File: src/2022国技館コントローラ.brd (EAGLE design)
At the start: 48 parts

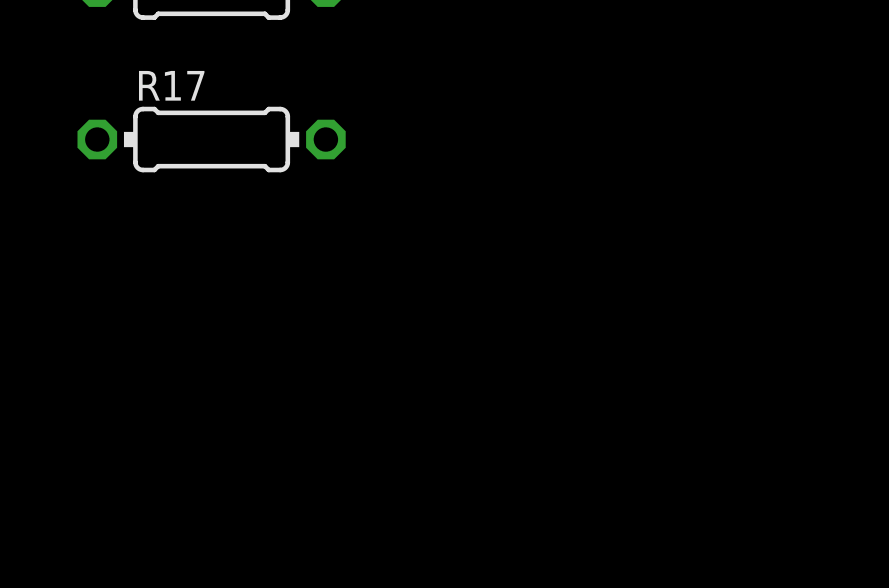
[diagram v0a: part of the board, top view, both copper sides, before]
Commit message: 国技館コントローラの追加
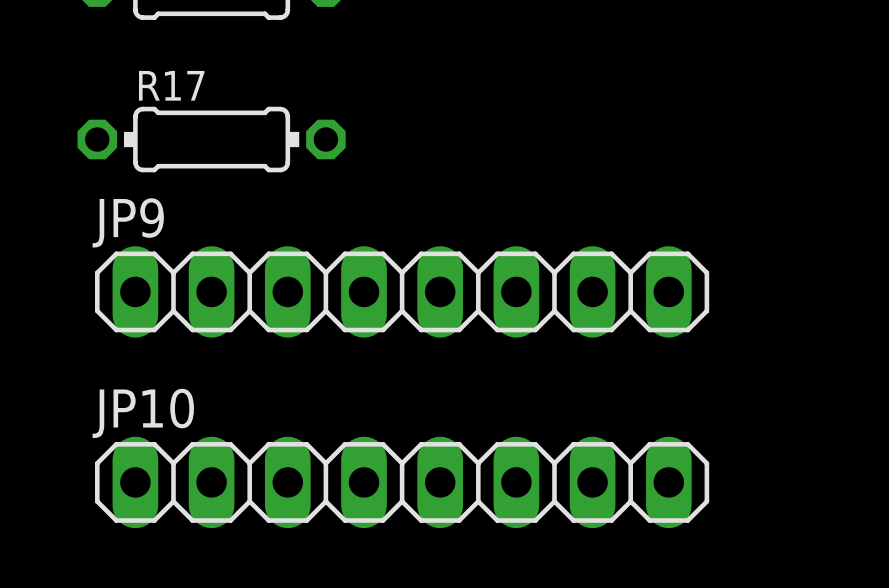
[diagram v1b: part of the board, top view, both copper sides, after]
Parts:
- added JP10, JP9: (no value), pinhead:1X08
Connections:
- new net BUSY: JP9.1
- new net RESET: JP9.8
- new net RX: JP9.4
- new net SLEEP: JP10.2
- new net STATUS: JP9.6
- new net TX: JP10.3
- new net VCC: JP9.7
- new net XMIT: JP9.2
- net GND: now also JP10.8
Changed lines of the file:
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@@
 <attribute name="VALUE" x="-181.9656" y="-156.6926" size="0.9906" layer="27" ratio="10"/>
+</element>
+<element name="JP9" library="pinhead" library_urn="urn:adsk.eagle:library:325" package="1X08" package3d_urn="urn:adsk.eagle:package:22409/2" value="" x="-173.99" y="-161.29" smashed="yes">
+<attribute name="NAME" x="-184.2262" y="-159.4612" size="1.27" layer="25" ratio="10"/>
+<attribute name="POPULARITY" value="67" x="-173.99" y="-161.29" size="1.778" layer="27" display="off"/>
+<attribute name="VALUE" x="-184.15" y="-164.465" size="1.27" layer="27"/>
+</element>
+<element name="JP10" library="pinhead" library_urn="urn:adsk.eagle:library:325" package="1X08" package3d_urn="urn:adsk.eagle:package:22409/2" value="" x="-173.99" y="-167.64" smashed="yes">
+<attribute name="NAME" x="-184.2262" y="-165.8112" size="1.27" layer="25" ratio="10"/>
+<attribute name="POPULARITY" value="67" x="-173.99" y="-167.64" size="1.778" layer="27" display="off"/>
+<attribute name="VALUE" x="-184.15" y="-170.815" size="1.27" layer="27"/>
 </element>
 </elements>
@@
 <contactref element="LED4" pad="K"/>
 <contactref element="LED5" pad="K"/>
+<contactref element="JP10" pad="8"/>
 <wire x1="-176.53" y1="-68.58" x2="-176.53" y2="-73.66" width="0" layer="19" extent="1-1"/>
 <wire x1="-176.53" y1="-63.5" x2="-176.53" y2="-68.58" width="0" layer="19" extent="1-1"/>
@@
 <wire x1="-180.34" y1="-121.92" x2="-180.34" y2="-114.3" width="0" layer="19" extent="1-1"/>
 <wire x1="-180.34" y1="-129.54" x2="-180.34" y2="-121.92" width="0" layer="19" extent="1-1"/>
+<wire x1="-165.1" y1="-167.64" x2="-180.34" y2="-129.54" width="0" layer="19" extent="1-1"/>
 <wire x1="-58.42" y1="-19.05" x2="-176.53" y2="-38.1" width="0" layer="19" extent="1-1"/>
 <wire x1="-58.42" y1="-11.43" x2="-58.42" y2="-19.05" width="0" layer="19" extent="1-1"/>
@@
 <contactref element="R17" pad="1"/>
 </signal>
+<signal name="BUSY">
+<contactref element="JP9" pad="1"/>
+</signal>
+<signal name="XMIT">
+<contactref element="JP9" pad="2"/>
+</signal>
+<signal name="TX">
+<contactref element="JP10" pad="3"/>
+</signal>
+<signal name="RX">
+<contactref element="JP9" pad="4"/>
+</signal>
+<signal name="STATUS">
+<contactref element="JP9" pad="6"/>
+</signal>
+<signal name="VCC">
+<contactref element="JP9" pad="7"/>
+</signal>
+<signal name="RESET">
+<contactref element="JP9" pad="8"/>
+</signal>
+<signal name="SLEEP">
+<contactref element="JP10" pad="2"/>
+</signal>
 </signals>

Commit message: 「ｋ」コントローラ
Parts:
- added JP11, JP12: (no value), con-jst-xh (1):B5B-XH
- added SV1, SV2: (no value), con-ml:ML10
- added U$15: 02-JST, con-jst-xh (1):B2B-XH
- moved U$14 331.8 mm to (134.6, 71.1), turned to 180 degrees
- moved R8 328.9 mm to (110.5, 80.0), turned to 270 degrees
- moved R7 327.7 mm to (113.0, 77.5), turned to 270 degrees
- moved R6 326.7 mm to (115.6, 74.9), turned to 270 degrees
- moved R5 325.9 mm to (118.1, 72.4), turned to 270 degrees
- moved U$13 324.5 mm to (134.6, 78.7), turned to 180 degrees
- moved U$10 279.0 mm to (111.8, 88.9), turned to 180 degrees
- moved U$9 276.7 mm to (119.4, 88.9), turned to 180 degrees
- moved U$8 274.4 mm to (127.0, 88.9), turned to 180 degrees
- moved U$7 272.1 mm to (134.6, 88.9), turned to 180 degrees
- moved R1 237.2 mm to (25.4, 80.0), turned to 270 degrees
- moved R2 236.3 mm to (22.9, 77.5), turned to 270 degrees
- moved R3 235.5 mm to (20.3, 74.9), turned to 270 degrees
- moved R4 234.6 mm to (17.8, 72.4), turned to 270 degrees
- moved LED1 219.2 mm to (-12.7, 40.6)
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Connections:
- removed net VCC: JP9.7
- new net VIN: F411RE_LEFT.24, U$15.2
- net 3V3: now also F411RE_LEFT.16, JP9.7, SV1.2, SV2.2
- net BL1: now also F411RE_RIGHT.11
- net BL2: now also F411RE_RIGHT.13
- net BR1: now also F411RE_RIGHT.23
- net BR2: now also F411RE_RIGHT.25
- net BUSY: now also F411RE_RIGHT.24, SV1.10, SV2.10
- net CK1_DOWN: now also F411RE_RIGHT.21, U$4.1; no longer U$5.1
- net CK1_LEFT: now also F411RE_RIGHT.15
- net CK1_RIGHT: now also F411RE_RIGHT.17, U$5.1; no longer U$6.1
- net CK1_UP: now also F411RE_RIGHT.19, U$6.1; no longer U$4.1
- net CK2_DOWN: now also F411RE_RIGHT.33, U$10.1; no longer U$9.1
- net CK2_LEFT: now also F411RE_RIGHT.27, U$7.1; no longer U$8.1
- net CK2_RIGHT: now also F411RE_RIGHT.29, U$9.1; no longer U$10.1
- net CK2_UP: now also F411RE_RIGHT.31, U$8.1; no longer U$7.1
- net GND: now also F411RE_LEFT.8, SV1.3, SV2.3, U$15.1
- net L/R1: now also F411RE_LEFT.28
- net L/R2: now also F411RE_LEFT.32
- net LED1: now also F411RE_RIGHT.1, JP11.1, JP12.1
- net LED2: now also F411RE_RIGHT.3, JP11.2, JP12.2
- net LED3: now also F411RE_RIGHT.5, JP11.3, JP12.3
- net LED4: now also F411RE_RIGHT.2, JP11.4, JP12.4
- net LED5: now also F411RE_RIGHT.4, JP11.5, JP12.5
- net RESET: now also F411RE_RIGHT.30, SV1.9, SV2.9
- net RX: now also F411RE_LEFT.21, SV1.6, SV2.6
- net SLEEP: now also F411RE_RIGHT.22, SV1.7, SV2.7
- net STATUS: now also F411RE_RIGHT.28, SV1.4, SV2.4
- net TX: now also F411RE_LEFT.17, SV1.5, SV2.5
- net U/D1: now also F411RE_LEFT.30
- net U/D2: now also F411RE_LEFT.34
- net XMIT: now also F411RE_RIGHT.26, SV1.8, SV2.8
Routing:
- net 3V3: track 0.00 -> 64.6 mm

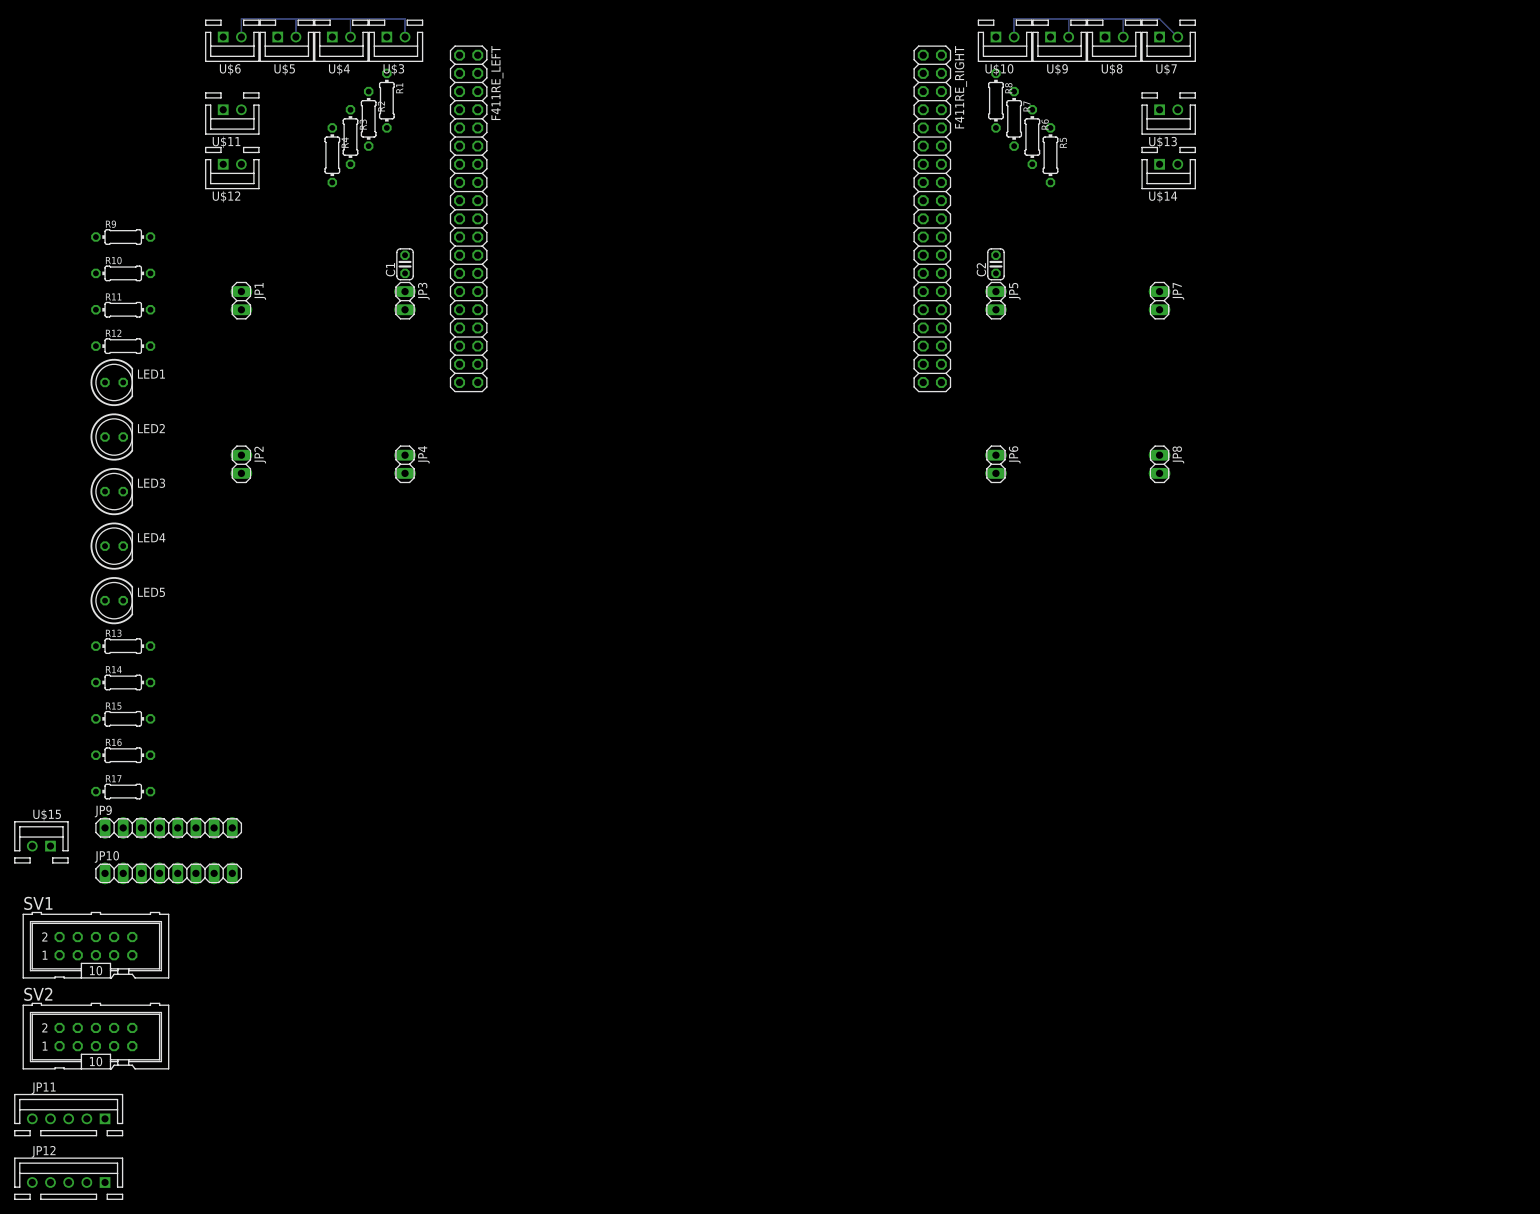
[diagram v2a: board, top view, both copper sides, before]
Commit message: 国技館コントローラ_配線の修正
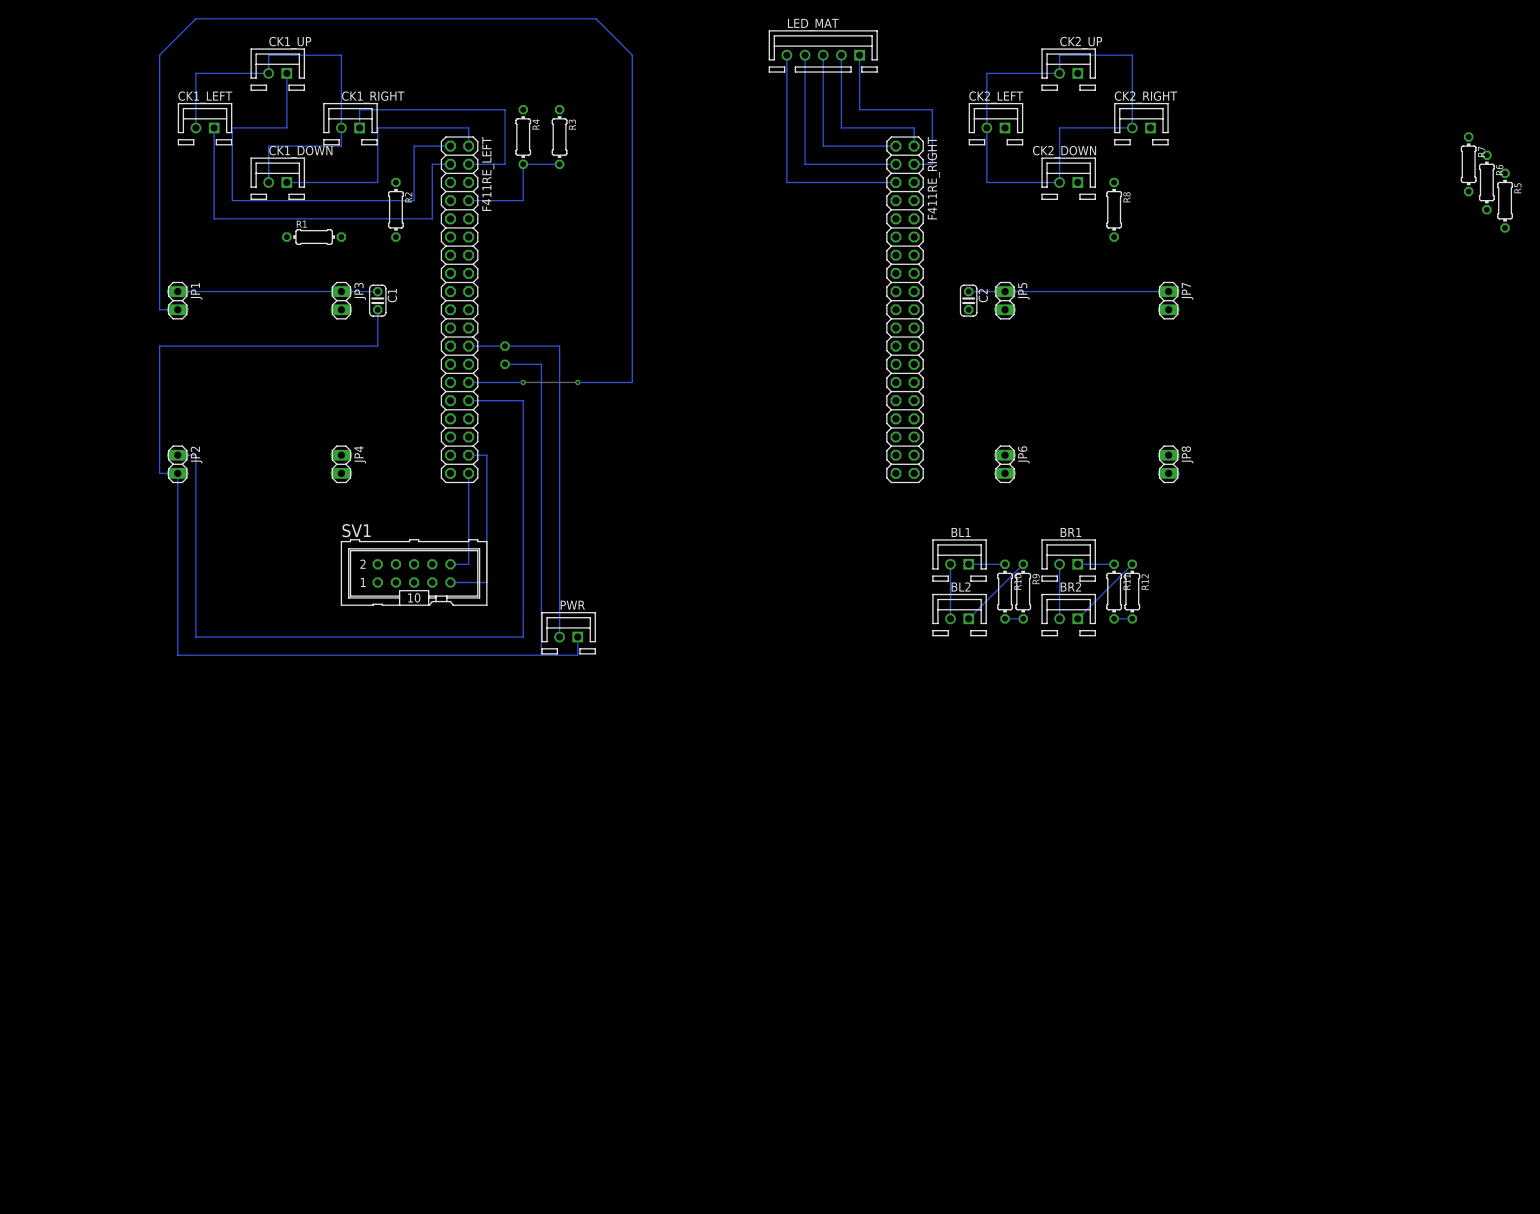
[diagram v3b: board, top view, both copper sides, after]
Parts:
- removed JP10, JP9: (no value), pinhead:1X08
- removed JP11, JP12: (no value), con-jst-xh (1):B5B-XH
- removed LED1, LED2, LED3, LED4, LED5: (no value), led:LED5MM
- removed R13, R14, R15, R16, R17: (no value), rcl:0204/7
- removed SV2: (no value), con-ml:ML10
- removed U$10, U$11, U$12, U$13, U$14, U$3, U$4, U$5, U$6, U$7, U$8, U$9: 02-JST, con-jst-xh:B2B-XH
- removed U$15: 02-JST, con-jst-xh (1):B2B-XH
- added BL1, BL2, BR1, BR2, CK1_DOWN, CK1_LEFT, CK1_RIGHT, CK1_UP, CK2_DOWN, CK2_LEFT, CK2_RIGHT, CK2_UP: 02-JST, con-jst-xh:B2B-XH
- added C3: 100nF, rcl:C025-024X044
- added LED_MAT: (no value), con-jst-xh (1):B5B-XH
- added PWR: 02-JST, con-jst-xh (1):B2B-XH
- R1, R10, R11, R12, R2, R3, R4, R5, R6, R7, R8, R9: value (none) -> 10k
- moved R12 145.1 mm to (129.5, 11.4), turned to 270 degrees
- moved R11 143.9 mm to (127.0, 11.4), turned to 270 degrees
- moved R9 135.1 mm to (114.3, 11.4), turned to 270 degrees
- moved R10 131.0 mm to (111.8, 11.4), turned to 270 degrees
- moved U$1 121.8 mm to (-8.89, 94.0), turned to 270 degrees
- moved U$2 118.6 mm to (68.6, 94.0), turned to 270 degrees
- moved SV1 68.5 mm to (29.2, 14.0)
- moved R5 63.8 mm to (181.6, 66.0)
- moved R6 63.8 mm to (179.1, 68.6)
- moved R7 63.8 mm to (176.5, 71.1)
- moved R3 29.2 mm to (49.5, 74.9)
- moved R4 26.8 mm to (44.5, 74.9)
- moved R8 22.5 mm to (127.0, 64.8)
- moved R1 21.6 mm to (15.2, 61.0), turned to 0 degrees
- moved R2 13.3 mm to (26.7, 64.8)
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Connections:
- removed net N$10: LED5.A, R17.2
- removed net N$6: LED1.A, R13.2
- removed net N$7: LED2.A, R14.2
- removed net N$8: LED3.A, R15.2
- removed net N$9: LED4.A, R16.2
- net 3V3: now also BL1.2, BL2.2, BR1.2, BR2.2, CK1_DOWN.2, CK1_LEFT.2, CK1_RIGHT.2, CK1_UP.2, CK2_DOWN.2, CK2_LEFT.2, CK2_RIGHT.2, CK2_UP.2; no longer JP9.7, SV2.2, U$10.2, U$11.2, U$12.2, U$13.2, U$14.2, U$3.2, U$4.2, U$5.2, U$6.2, U$7.2, U$8.2, U$9.2
- net BL1: now also BL1.1; no longer U$11.1
- net BL2: now also BL2.1; no longer U$12.1
- net BR1: now also BR1.1; no longer U$13.1
- net BR2: now also BR2.1; no longer U$14.1
- net BUSY: now also F411RE_LEFT.38; no longer F411RE_RIGHT.24, JP9.1, SV2.10
- net CK1_DOWN: now also CK1_DOWN.1, F411RE_LEFT.2; no longer F411RE_RIGHT.21, U$4.1
- net CK1_LEFT: now also CK1_LEFT.1, F411RE_LEFT.3; no longer F411RE_RIGHT.15, U$3.1
- net CK1_RIGHT: now also CK1_RIGHT.1, F411RE_LEFT.4; no longer F411RE_RIGHT.17, U$5.1
- net CK1_UP: now also CK1_UP.1, F411RE_LEFT.1; no longer F411RE_RIGHT.19, U$6.1
- net CK2_DOWN: now also CK2_DOWN.1; no longer U$10.1
- net CK2_LEFT: now also CK2_LEFT.1; no longer U$7.1
- net CK2_RIGHT: now also CK2_RIGHT.1; no longer U$9.1
- net CK2_UP: now also CK2_UP.1; no longer U$8.1
- net GND: now also C3.2, PWR.1; no longer JP10.8, LED1.K, LED2.K, LED3.K, LED4.K, LED5.K, SV2.3, U$15.1
- net LED1: now also F411RE_RIGHT.5, LED_MAT.5; no longer F411RE_RIGHT.1, JP11.1, JP12.1, R13.1
- net LED2: now also LED_MAT.4; no longer JP11.2, JP12.2, R14.1
- net LED3: now also F411RE_RIGHT.1, LED_MAT.3; no longer F411RE_RIGHT.5, JP11.3, JP12.3, R15.1
- net LED4: now also LED_MAT.2; no longer JP11.4, JP12.4, R16.1
- net LED5: now also LED_MAT.1; no longer JP11.5, JP12.5, R17.1
- net RESET: now also F411RE_LEFT.36; no longer F411RE_RIGHT.30, JP9.8, SV2.9
- net RX: no longer JP9.4, SV2.6
- net SLEEP: now also F411RE_LEFT.35; no longer F411RE_RIGHT.22, JP10.2, SV2.7
- net STATUS: now also F411RE_LEFT.37; no longer F411RE_RIGHT.28, JP9.6, SV2.4
- net TX: no longer JP10.3, SV2.5
- net VIN: now also C3.1, PWR.2; no longer U$15.2
- net XMIT: now also F411RE_LEFT.31; no longer F411RE_RIGHT.26, JP9.2, SV2.8
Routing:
- net GND: track 0.00 -> 208.3 mm
- net L/R1: track 0.00 -> 176.9 mm, vias 0 -> 2
- net 3V3: track 64.6 -> 205.7 mm
- net U/D1: track 0.00 -> 114.3 mm
- net CK1_UP: track 0.00 -> 63.5 mm
- net CK1_LEFT: track 0.00 -> 53.3 mm
- net VIN: track 0.00 -> 53.3 mm
- net CK1_DOWN: track 0.00 -> 35.6 mm
- net CK1_RIGHT: track 0.00 -> 35.6 mm
- net LED1: track 0.00 -> 33.0 mm
- net LED2: track 0.00 -> 27.9 mm
- net LED5: track 0.00 -> 27.9 mm
- net RESET: track 0.00 -> 25.4 mm
- net LED4: track 0.00 -> 22.9 mm
- net LED3: track 0.00 -> 22.9 mm
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
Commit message: [k]コントローラ
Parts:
- added U$3, U$4: 02-JST, con-jst-xh (1):B2B-XH
- moved R5 52.2 mm to (129.5, 62.2)
- moved R6 47.1 mm to (132.1, 64.8)
- moved R7 42.1 mm to (134.6, 67.3)
- moved R1 31.4 mm to (44.5, 72.4), turned to 270 degrees
- moved R2 16.1 mm to (41.9, 69.8)
- moved LED_MAT 7.62 mm to (86.4, 78.7)
- moved R10 5.68 mm to (109.2, 16.5)
- moved R9 5.68 mm to (111.8, 16.5)
- moved BL1 5.68 mm to (102.9, 20.3)
- moved BL2 5.68 mm to (102.9, 12.7)
- moved R11 5.08 mm to (127.0, 16.5)
- moved R12 5.08 mm to (129.5, 16.5)
- moved BR1 5.08 mm to (120.7, 20.3)
- moved BR2 5.08 mm to (120.7, 12.7)
- moved R8 5.08 mm to (127.0, 59.7)
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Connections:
- net 3V3: now also F411RE_RIGHT.7, SV1.3; no longer SV1.2
- net BL1: now also F411RE_RIGHT.28; no longer F411RE_RIGHT.11
- net BL2: now also F411RE_RIGHT.30; no longer F411RE_RIGHT.13
- net BR1: now also F411RE_RIGHT.24; no longer F411RE_RIGHT.23
- net BR2: now also F411RE_RIGHT.26; no longer F411RE_RIGHT.25
- net GND: now also F411RE_LEFT.19, F411RE_LEFT.22, F411RE_RIGHT.20, SV1.7; no longer SV1.3
- net L/R2: now also U$3.2, U$4.2
- net RX: now also SV1.2; no longer SV1.6
- net SLEEP: now also SV1.6; no longer SV1.7
- net STATUS: now also SV1.8; no longer SV1.4
- net U/D2: now also U$3.1, U$4.1
- net XMIT: now also SV1.4; no longer SV1.8
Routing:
- net 3V3: track 205.7 -> 576.1 mm, vias 0 -> 6
- net GND: track 208.3 -> 458.4 mm
- net CK2_UP: track 0.00 -> 191.1 mm, vias 0 -> 2
- net L/R2: track 0.00 -> 178.9 mm, vias 0 -> 4
- net CK2_DOWN: track 0.00 -> 169.7 mm, vias 0 -> 2
- net CK2_LEFT: track 0.00 -> 167.6 mm, vias 0 -> 2
- net CK2_RIGHT: track 0.00 -> 147.3 mm
- net TX: track 0.00 -> 109.2 mm, vias 0 -> 2
- net U/D2: track 0.00 -> 84.9 mm, vias 0 -> 4
- net BR2: track 10.8 -> 73.7 mm
- net BR1: track 5.08 -> 53.3 mm
- net RX: track 0.00 -> 40.6 mm
- net BL2: track 10.8 -> 45.7 mm, vias 0 -> 2
- net CK1_UP: track 63.5 -> 94.0 mm, vias 0 -> 2
- net CK1_LEFT: track 53.3 -> 81.3 mm, vias 0 -> 2
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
